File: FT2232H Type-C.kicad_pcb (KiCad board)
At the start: 2 copper layers, 52 x 40 mm, 34 parts, among them J1 CONN_01X20, J2 CONN_01X20, J3 USB_TYPE_C, U1 LD1117S33TR, U3 93CxxB, U4 FT2232H, Y1 12Mhz

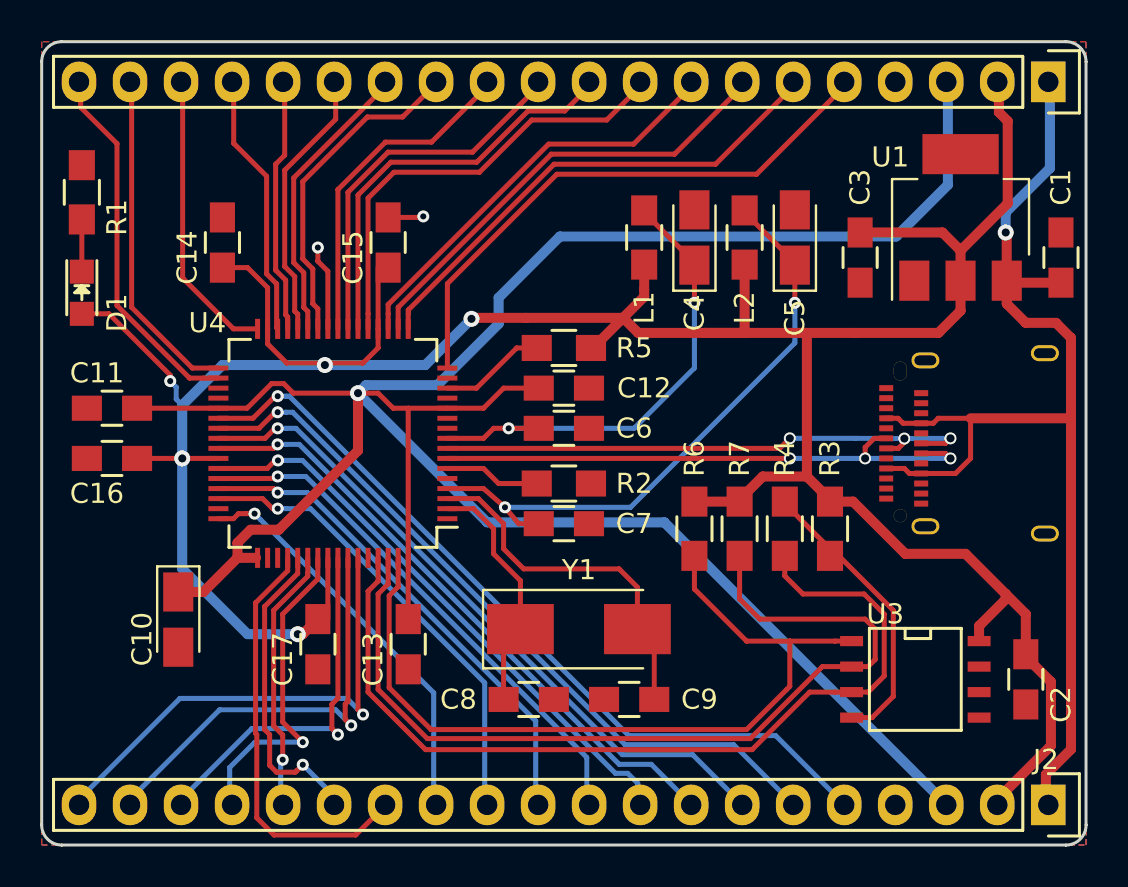
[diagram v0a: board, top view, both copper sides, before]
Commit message: Fix routing and add REGIN capacitor
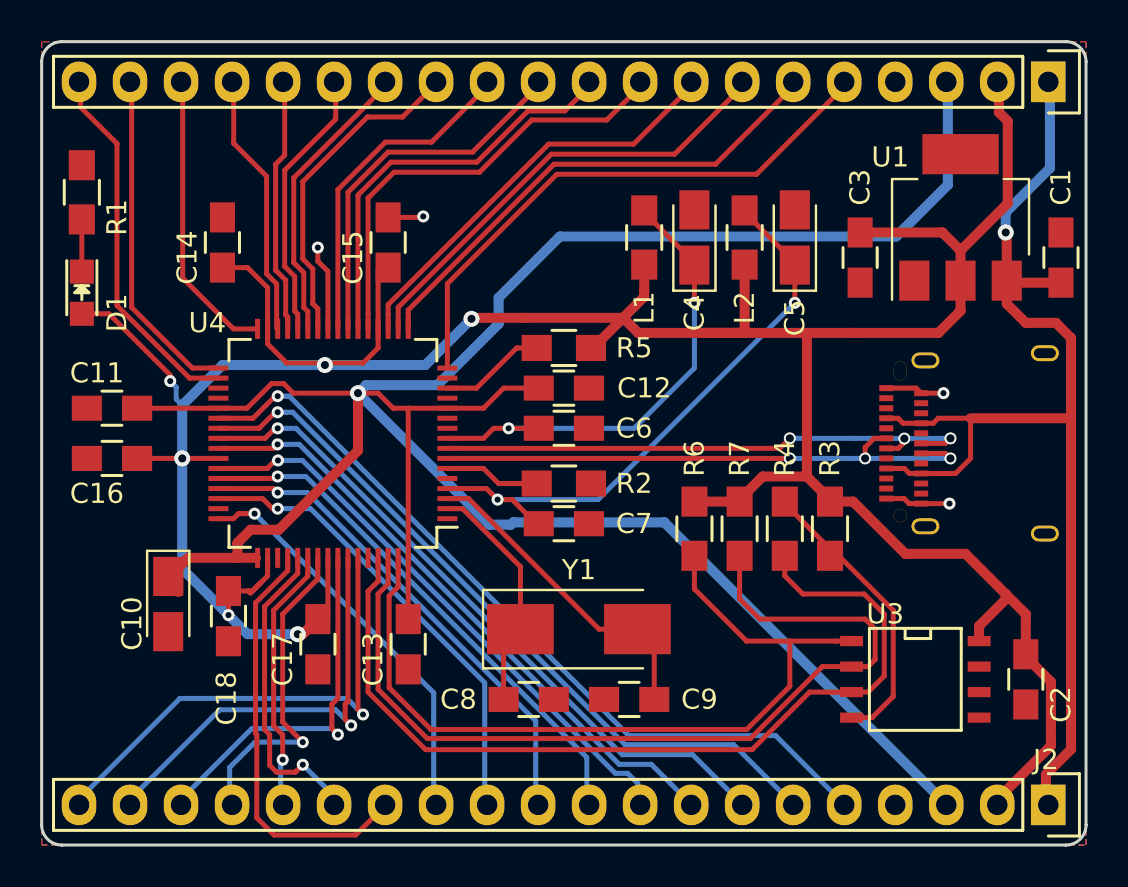
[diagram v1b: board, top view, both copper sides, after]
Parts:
- added C18: 0.1uF, Capacitors_SMD:C_0805_HandSoldering, F.Cu at (157.3, 108.6)
- moved C10 0.92 mm to (154.3, 108.0)
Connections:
- J3 pad A10: Net-(J3-PadA10) -> (no net)
- J3 pad A11: Net-(J3-PadA11) -> (no net)
- J3 pad A2: Net-(J3-PadA2) -> (no net)
- J3 pad A3: Net-(J3-PadA3) -> (no net)
- J3 pad A5: Net-(J3-PadA5) -> (no net)
- J3 pad A8: Net-(J3-PadA8) -> (no net)
- J3 pad B10: Net-(J3-PadB10) -> (no net)
- J3 pad B11: Net-(J3-PadB11) -> (no net)
- J3 pad B2: Net-(J3-PadB2) -> (no net)
- J3 pad B3: Net-(J3-PadB3) -> (no net)
- J3 pad B5: Net-(J3-PadB5) -> (no net)
- J3 pad B8: Net-(J3-PadB8) -> (no net)
- U3 pad 6: Net-(U3-Pad6) -> (no net)
- U3 pad 7: Net-(U3-Pad7) -> (no net)
- U4 pad 36: Net-(U4-Pad36) -> (no net)
- U4 pad 60: Net-(U4-Pad60) -> (no net)
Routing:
- net GND: track 6.03 -> 12.2 mm, vias 2 -> 4
- net +3V3: track 157.9 -> 163.1 mm, vias 5 -> 6
- net Net-(C9-Pad1): track 18.0 -> 16.0 mm
- net Net-(C5-Pad1): track 30.7 -> 29.8 mm
- net +1V8: track 125.3 -> 126.1 mm
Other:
- board text added: "FT2232H Type-C Breakout Board v0.2 Charles-Xavier Roy, Oct 2017"
- board text removed: "FT2232H Type-C Breakout Board Charles-Xavier Roy, Aug 2017"

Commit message: Update USB-C connector to check chinease version
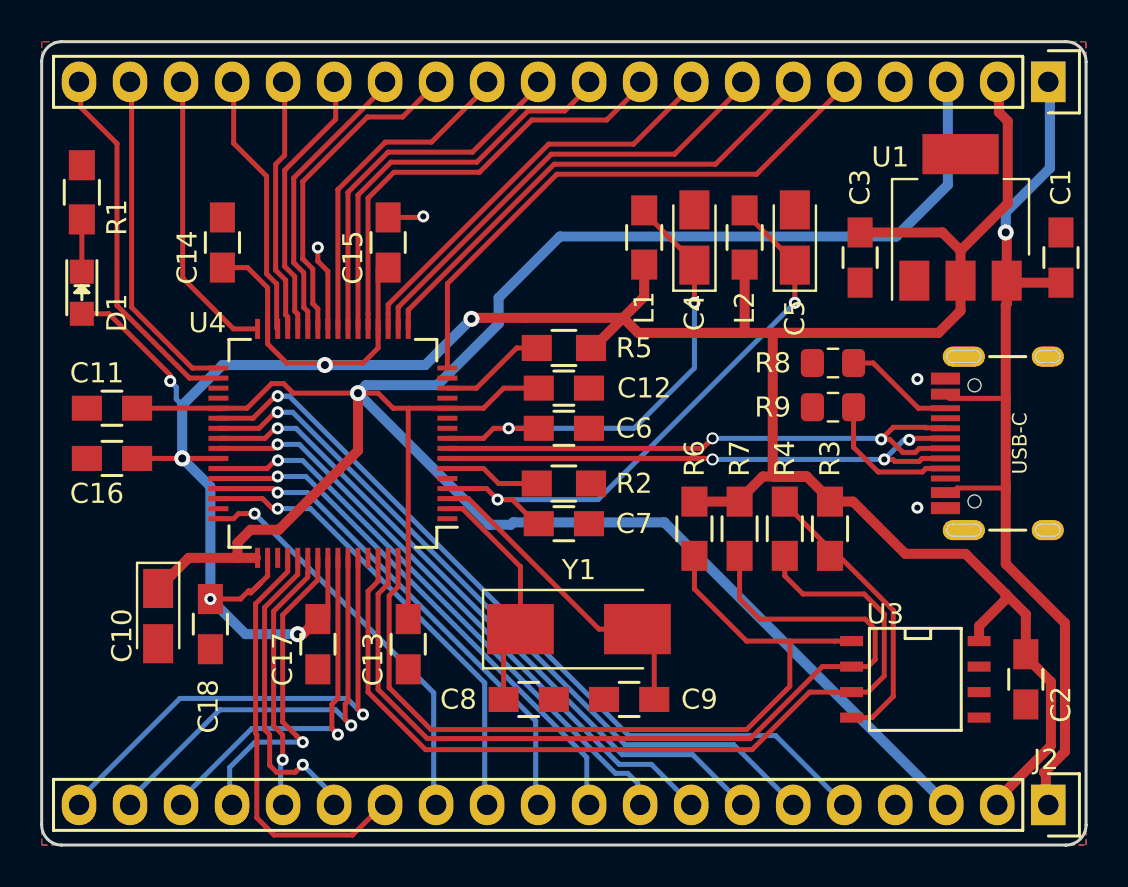
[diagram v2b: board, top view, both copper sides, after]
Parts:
- added R8: 5.1k, Resistor_SMD:R_0805_2012Metric_Pad1.15x1.40mm_HandSolder, F.Cu at (187.4, 96.0)
- added R9: 5.1k, Resistor_SMD:R_0805_2012Metric_Pad1.15x1.40mm_HandSolder, F.Cu at (187.4, 98.2)
- J3: value USB_TYPE_C -> USB_C16PIN; footprint Land Patterns:12401598E4#2ACT-ND -> USB-C-COM-15111:USB-C-COM-15111
- moved J3 2.25 mm to (193.0, 100.0)
- moved C18 0.98 mm to (156.4, 109.0)
- moved C10 0.78 mm to (153.8, 108.6)
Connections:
- J3 pad A5: (no net) -> Net-(J3-PadA5)
- J3 pad B5: (no net) -> Net-(J3-PadB5)
- U3 pad 6: (no net) -> Net-(U3-Pad6)
- U3 pad 7: (no net) -> Net-(U3-Pad7)
- U4 pad 36: (no net) -> Net-(U4-Pad36)
- U4 pad 60: (no net) -> Net-(U4-Pad60)
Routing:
- net +5V: track 58.4 -> 47.6 mm
- net Net-(J3-PadA5): track 0.00 -> 7.15 mm
- net GND: track 12.2 -> 6.03 mm
- net Net-(J3-PadB5): track 0.00 -> 5.51 mm
- net +3V3: track 163.1 -> 166.2 mm
- net /D+: track 28.0 -> 28.8 mm, vias 3 -> 2
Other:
- board text added: "FT2232H Type-C Breakout Board v0.3 Charles-Xavier Roy, August 2020"
- board text removed: "FT2232H Type-C Breakout Board v0.2 Charles-Xavier Roy, Oct 2017"
